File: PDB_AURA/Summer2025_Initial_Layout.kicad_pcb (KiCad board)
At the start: 4 copper layers, 50 x 100 mm, 123 parts, among them J10 532617006, J100 XT30PW-M, J101 USB_C_Receptacle_USB2.0_16P, J3 532617004, J4 TF-CARD_H1.8, J400 Screw_Terminal_01x04, J5 TSW-108-07-G-T, J6 532617004, Q1 BSS138, Q2 BSS138, U1 SI4825DDY-T1-GE3, U101 TPS2115ADRBR, U102 TLV62566DBVR, U103 AP2127N-1.8, U11 ICM-20948, U12 BMP280, U13 MAX-M10S, U2 RFM95W-868S2, U200 ESP32-S3-WROOM-1, U201 USBLC6-2SC6, U3 TPS56C230RJER, U400 DMN6040SSD-13

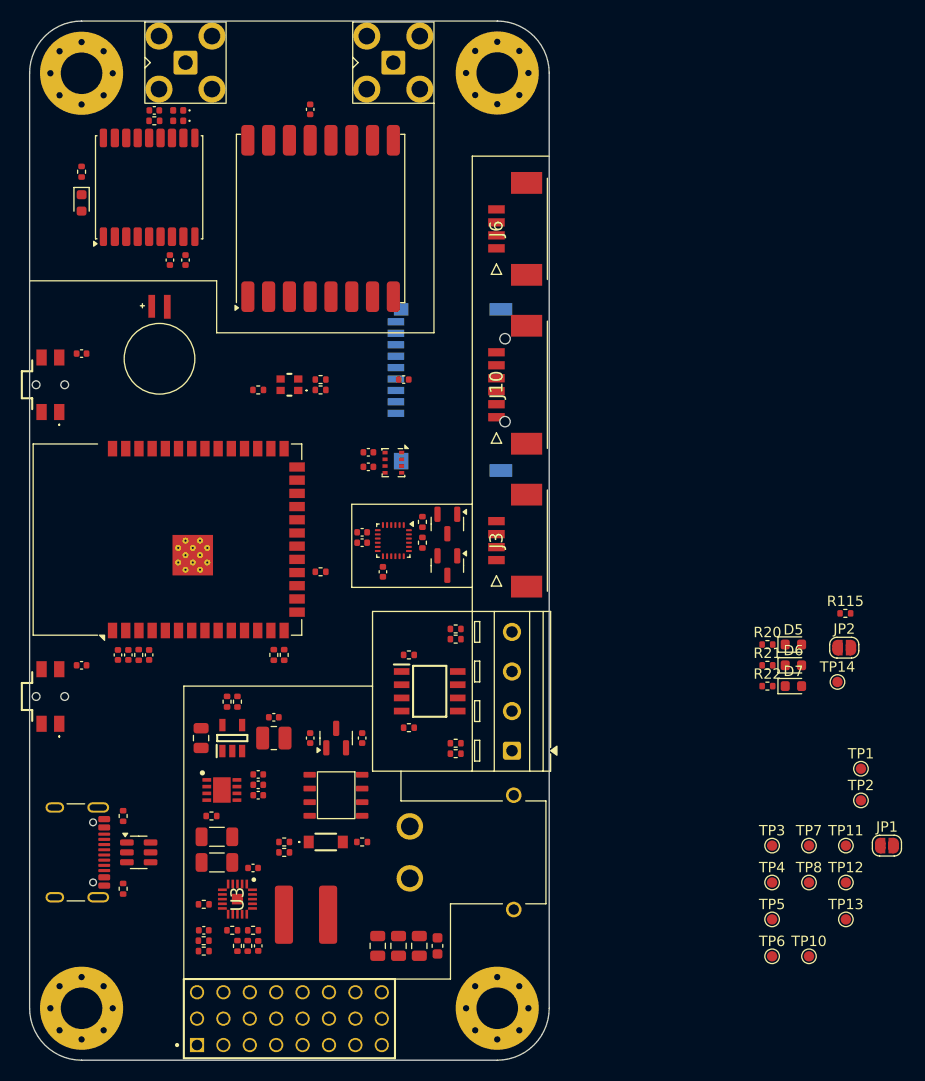
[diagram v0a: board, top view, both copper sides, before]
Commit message: Annotated schematic for PDB
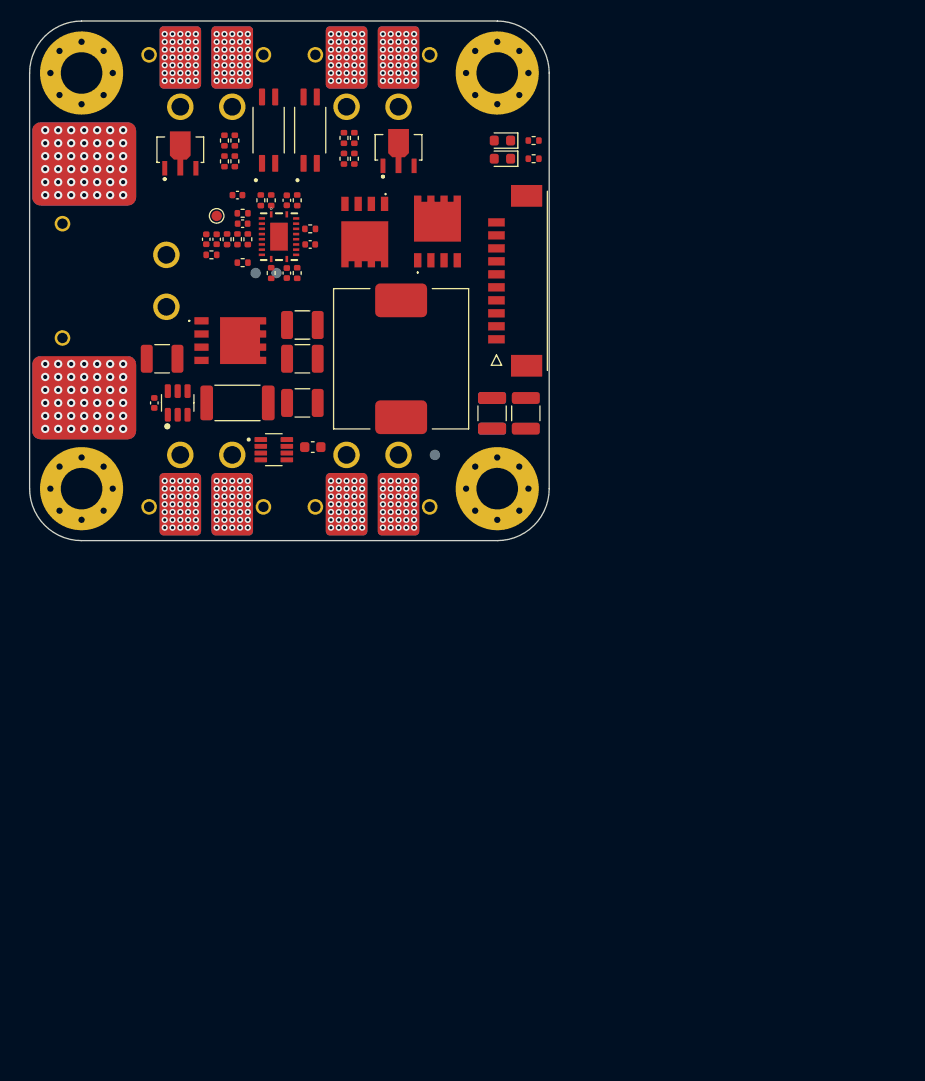
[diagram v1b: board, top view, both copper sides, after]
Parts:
- removed BT1: MS621FE-FL11E, BAT_MS621FE-FL11E:BAT_MS621FE-FL11E
- removed C100, C113, C114: 1u, Capacitor_SMD:C_0402_1005Metric
- removed C101, C102: 22u, Capacitor_SMD:C_1206_3216Metric
- removed C103: 18n, Capacitor_SMD:C_0402_1005Metric
- removed C104, C108, C109, C201, C203, C204, C22, C25, C27, C38, C39, C41, C42, C43, C44, C45: 100n, Capacitor_SMD:C_0402_1005Metric
- removed C105, C106, C107: 22u, Capacitor_SMD:C_0805_2012Metric
- removed C110, C112, C202: 10u, Capacitor_SMD:C_0402_1005Metric
- removed C111: 4u7, Capacitor_SMD:C_0805_2012Metric
- removed C115: 100n, Capacitor_SMD:C_0603_1608Metric
- removed D4, D5, D6, D7: LED, LED_SMD:LED_0603_1608Metric
- removed D503490: ~, Diode_SMD:D_0402_1005Metric
- removed J101: USB_C_Receptacle_USB2.0_16P, Connector_USB:USB_C_Receptacle_GCT_USB4105-xx-A_16P_TopMnt_Horizontal
- removed J400: Screw_Terminal_01x04, TerminalBlock_MetzConnect:TerminalBlock_MetzConnect_Type086_RT03404HBLC_1x04_P3.81mm_Horizontal
- removed JP1, JP2: SolderJumper_2_Bridged, Jumper:SolderJumper-2_P1.3mm_Open_RoundedPad1.0x1.5mm
- removed L100: 1u8, CKST0603:CKST0603-1.5uHM
- removed L101: 2u2, Inductor_SMD:L_1008_2520Metric
- removed L4: 27nH, LED_SMD:LED_0402_1005Metric
- removed R100: 100k, Resistor_SMD:R_0402_1005Metric
- removed R101: 49k, Resistor_SMD:R_0402_1005Metric
- removed R102: 13k, Resistor_SMD:R_0402_1005Metric
- removed R103: 180k, Resistor_SMD:R_0402_1005Metric
- removed R104: 33k, Resistor_SMD:R_0402_1005Metric
- removed R105: 330k, Resistor_SMD:R_0402_1005Metric
- removed R106: 110k, Resistor_SMD:R_0402_1005Metric
- removed R107: 15k, Resistor_SMD:R_0402_1005Metric
- removed R108, R109: 5k1, Resistor_SMD:R_0402_1005Metric
- removed R110: 680R, Resistor_SMD:R_0402_1005Metric
- removed R111: 540k, Resistor_SMD:R_0402_1005Metric
- removed R113, R115, R400, R403: 220k, Resistor_SMD:R_0402_1005Metric
- removed R114, R401, R404: 22k, Resistor_SMD:R_0402_1005Metric
- removed R18, R19, R22: 1k, Resistor_SMD:R_0402_1005Metric
- removed R20, R21: 4k7, Resistor_SMD:R_0402_1005Metric
- removed R25, R26, R27, R402, R405: 10k, Resistor_SMD:R_0402_1005Metric
- removed R36: 100R, Resistor_SMD:R_0402_1005Metric
- removed R37: 120R, Resistor_SMD:R_0402_1005Metric
- removed R38: 270R, Resistor_SMD:R_0402_1005Metric
- removed S3, S4: EVQ-PUC02K, SamacSys_Parts:EVQPUC02K
- removed TP10, TP11, TP12, TP13, TP14, TP5, TP6, TP7, TP8: TestPoint, TestPoint:TestPoint_Pad_D1.0mm
- removed U101: TPS2115ADRBR, SamacSys_Parts:SON65P300X300X100-9N-D
- removed U102: TLV62566DBVR, SamacSys_Parts:SOT95P280X145-5N
- removed U103: AP2127N-1.8, Package_TO_SOT_SMD:SOT-23
- removed U11: ICM-20948, Sensor_Motion:InvenSense_QFN-24_3x3mm_P0.4mm
- removed U12: BMP280, Package_LGA:Bosch_LGA-8_2x2.5mm_P0.65mm_ClockwisePinNumbering
- removed U13: MAX-M10S, RF_GPS:ublox_MAX
- removed U3: TPS56C230RJER, SamacSys_Parts:QFN45P300X300X100-21N-D
- removed U400: DMN6040SSD-13, SamacSys_Parts:SOIC127P600X170-8N
- added C1: 1n, Capacitor_SMD:C_0402_1005Metric, F.Cu at (67.0, 71.0)
- added C10: 47u, Capacitor_SMD:C_1210_3225Metric, F.Cu at (76.2, 86.8)
- added C11: 22u, Capacitor_SMD:C_1210_3225Metric, F.Cu at (76.2, 79.2)
- added C12: 22u, Capacitor_SMD:C_1210_3225Metric, F.Cu at (62.8, 82.5)
- added C14: 22u, Capacitor_SMD:C_1210_3225Metric, F.Cu at (94.5, 87.8)
- added C15: 22u, Capacitor_SMD:C_1210_3225Metric, B.Cu at (94.5, 87.8)
- added C16: 22u, Capacitor_SMD:C_1210_3225Metric, F.Cu at (76.2, 82.5)
- added C2: 8n2, Capacitor_SMD:C_0402_1005Metric, F.Cu at (70.0, 66.8)
- added C3: 100n, Capacitor_SMD:C_0402_1005Metric, F.Cu at (70.5, 69.5)
- added C4: 390p, Capacitor_SMD:C_0402_1005Metric, F.Cu at (68.0, 71.0)
- added C4: 390p, Capacitor_SMD:C_0402_1005Metric, F.Cu at (62.0, 86.8)
- added C5: 100n, Resistor_SMD:R_0402_1005Metric, F.Cu at (77.0, 70.0)
- added C6: 2u2, Capacitor_SMD:C_0402_1005Metric, F.Cu at (77.0, 71.5)
- added C7: 10p, Capacitor_SMD:C_0402_1005Metric, F.Cu at (74.8, 74.2)
- added C8: 100n, Capacitor_SMD:C_0402_1005Metric, F.Cu at (74.8, 67.2)
- added C9: 22u, Capacitor_SMD:C_1210_3225Metric, F.Cu at (97.8, 87.8)
- added J200: 532617010, 532617010:532617010, F.Cu at (94.9, 75.0)
- added J201: XT30PW-F, XT30PWF:XT30PWF, F.Cu at (64.5, 58.2)
- added J202: XT30PW-F, XT30PWF:XT30PWF, F.Cu at (80.5, 58.2)
- added J203: XT30PW-F, XT30PWF:XT30PWF, F.Cu at (69.5, 91.8)
- added J204: XT30PW-F, XT30PWF:XT30PWF, F.Cu at (85.5, 91.8)
- added J7: ~, SOLDER_PAD:PWR_SOLDER_PAD, B.Cu at (80.5, 53.5)
- added J8: ~, SOLDER_PAD:PWR_SOLDER_PAD, B.Cu at (80.5, 96.5)
- added J9: ~, SOLDER_PAD:BAT_SOLDER_PAD, F.Cu at (55.2, 86.2)
- added L1: 1u8, 125CDMCCDS-1R8MC:Untitled, F.Cu at (85.8, 82.5)
- added Q200: HSK10N06, HSK10N06:HSK10N06, F.Cu at (64.5, 63.6)
- added Q201: HSK10N06, HSK10N06:HSK10N06, F.Cu at (85.5, 63.4)
- added Q3: CSD18540Q5B, CSD18540Q5B:CSD18540Q5B, F.Cu at (69.3, 80.8)
- added R1: 18k, Resistor_SMD:R_0402_1005Metric, F.Cu at (70.0, 71.0)
- added R10: 9k1, Resistor_SMD:R_0402_1005Metric, F.Cu at (72.2, 67.2)
- added R11: 2R1, Resistor_SMD:R_0402_1005Metric, F.Cu at (75.8, 67.2)
- added R12: 0m5, Resistor_SMD:R_2512_6332Metric, F.Cu at (70.0, 86.8)
- added R13: 4k7, Resistor_SMD:R_0402_1005Metric, F.Cu at (98.5, 61.5)
- added R2: 3k4, Resistor_SMD:R_0402_1005Metric, F.Cu at (71.0, 71.0)
- added R203: 100R, Resistor_SMD:R_0402_1005Metric, F.Cu at (68.8, 61.5)
- added R204: 10k, Resistor_SMD:R_0402_1005Metric, F.Cu at (81.2, 61.2)
- added R205: 470R, Resistor_SMD:R_0402_1005Metric, F.Cu at (81.2, 63.2)
- added R206: 10k, Resistor_SMD:R_0402_1005Metric, F.Cu at (80.2, 61.2)
- added R207: 100R, Resistor_SMD:R_0402_1005Metric, F.Cu at (80.2, 63.2)
- added R3: 1k47, Resistor_SMD:R_0402_1005Metric, F.Cu at (69.0, 71.0)
- added R4: 4k7, Resistor_SMD:R_0402_1005Metric, F.Cu at (70.5, 68.5)
- added R5: 249R, Resistor_SMD:R_0402_1005Metric, F.Cu at (67.5, 72.5)
- added R6: 20k, Resistor_SMD:R_0402_1005Metric, F.Cu at (70.5, 73.2)
- added R7: 576R, Resistor_SMD:R_0402_1005Metric, F.Cu at (75.8, 74.2)
- added R8: 4k7, Resistor_SMD:R_0402_1005Metric, F.Cu at (73.2, 74.2)
- added R9: 35k7, Resistor_SMD:R_0402_1005Metric, F.Cu at (73.2, 67.2)
- added U202: INA219AIDCNR, INA219AIDCNR:SOT65P280X145-8N, F.Cu at (73.5, 91.2)
- C200: value 22u -> 100n; footprint Capacitor_SMD:C_0402_1005Metric -> Capacitor_SMD:C_0603_1608Metric
- D1: value NH-B2020RGBA-HF -> LED; footprint SamacSys_Parts:NHB2020RGBAHF -> LED_SMD:LED_0603_1608Metric
- D101: value MMSZ5242B -> LED; footprint SamacSys_Parts:MMSZ5252B -> LED_SMD:LED_0603_1608Metric
- J1, J2: footprint SMA_Connector:SMA_Connector -> SOLDER_PAD:PWR_SOLDER_PAD; moved to B.Cu
- J10: value 532617006 -> ~; footprint SamacSys_Parts:532617006 -> SOLDER_PAD:BAT_SOLDER_PAD
- J100: footprint SamacSys_Parts:XT30PWM -> XT30PWM:XT30PWM
- J3, J6: value 532617004 -> ~; footprint SamacSys_Parts:532617004 -> SOLDER_PAD:PWR_SOLDER_PAD; moved to B.Cu
- J4: value TF-CARD_H1.8 -> ~; footprint SamacSys_Parts:TFCARDH18 -> SOLDER_PAD:PWR_SOLDER_PAD
- J5: value TSW-108-07-G-T -> ~; footprint SAMTEC_TSW-108-07-G-T:SAMTEC_TSW-108-07-G-T -> SOLDER_PAD:PWR_SOLDER_PAD; moved to B.Cu
- Q1: value BSS138 -> CSD18540Q5B; footprint Package_TO_SOT_SMD:SOT-23 -> CSD18540Q5B:CSD18540Q5B
- Q2: value BSS138 -> CSD18510Q5B; footprint Package_TO_SOT_SMD:SOT-23 -> CSD18510Q5B:CSD18540Q5BT
- R112: value 120k -> 4k7
- R201: value 0R -> 470R
- R202: value 0R -> 10k
- TP1, TP3, TP4: moved to B.Cu
- U1: value SI4825DDY-T1-GE3 -> LM25145RGYR; footprint SI4825DDY-T1-GE3:SI4825DDY-T1-GE3 -> LM24145RGYR:RGY0020B
- U2: value RFM95W-868S2 -> LM74700; footprint RF_Module:HOPERF_RFM9XW_SMD -> Package_TO_SOT_SMD:SOT-23-6
- U200: value ESP32-S3-WROOM-1 -> LTV-217-B-G; footprint RF_Module:ESP32-S3-WROOM-1 -> LTV-217-B-G:SOIC127P700X210-4N
- U201: value USBLC6-2SC6 -> LTV-217-B-G; footprint Package_TO_SOT_SMD:SOT-23-6 -> LTV-217-B-G:SOIC127P700X210-4N
- moved H3 90.0 mm to (55.0, 55.0)
- moved H4 90.0 mm to (95.0, 55.0)
- moved TP2 83.7 mm to (68.0, 68.8)
- moved TP1 75.3 mm to (71.8, 74.2), turned to 180 degrees
- moved TP3 72.9 mm to (73.8, 74.2), turned to 180 degrees
- moved U201 71.4 mm to (77.0, 60.5), turned to 90 degrees
- moved D101 67.9 mm to (95.5, 63.2), turned to 180 degrees
- moved J100 65.3 mm to (57.2, 75.0), turned to 90 degrees
- moved R112 60.0 mm to (98.5, 63.2), turned to 180 degrees
- moved H1 56.6 mm to (55.0, 95.0)
- moved H2 56.6 mm to (95.0, 95.0)
- moved J3 55.6 mm to (64.5, 53.5), turned to 180 degrees
- moved U1 54.0 mm to (74.0, 70.8), turned to 0 degrees
- moved TP4 52.4 mm to (89.0, 91.8), turned to 180 degrees
- moved J5 50.6 mm to (85.5, 96.5), turned to 180 degrees
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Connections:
- D1 pad 1: LED_R -> /100_Power/5V_LED
- D1 pad 2: LED_B -> +5V
- D101 pad 1: +BATT_FILT -> /100_Power/VBAT_LED
- D101 pad 2: /Power/rvrs_plr -> +BATT_FILT
- J1 pad 1: /RF_Peripherals/LORA_ANT -> +BATT_FILT
- J10 pad 1: +3V3 -> GND
- J2 pad 1: /RF_Peripherals/GPS_RF_IN -> GND
- J3 pad 1: +3V3 -> +BATT_FILT
- J4 pad 1: unconnected-(J4-DAT2-Pad1) -> GND
- J6 pad 1: TCK -> GND
- Q1 pad 1: +1V8 -> /100_Power/5V_HO
- Q1 pad 2: /Digital_Peripherals/SCL_1V8 -> +BATT_FILT
- Q1 pad 3: SCL -> /100_Power/5V_SW
- Q2 pad 1: +1V8 -> /100_Power/5V_LO
- Q2 pad 2: /Digital_Peripherals/SDA_1V8 -> /100_Power/5V_SW
- Q2 pad 3: SDA -> GND
- R112 pad 2: /Power/FB_3V3 -> /100_Power/VBAT_LED
- R200 pad 1: /ESP32/EN -> GND
- R200 pad 2: +3V3 -> MSFT_1
- R201 pad 1: /ESP32/USB_MCU_D- -> /200_Connectors/MSFT_1_R
- R201 pad 2: /ESP32/D- -> MSFT_1
- R202 pad 1: /ESP32/USB_MCU_D+ -> GND
- R202 pad 2: /ESP32/D+ -> /200_Connectors/VGS_CH1
- TP1 pad 1: /Digital_Peripherals/SCL_1V8 -> /100_Power/5V_SYNCOUT
- TP2 pad 1: /Digital_Peripherals/SDA_1V8 -> /100_Power/5V_FB
- TP3 pad 1: /Power/PGOOD -> /100_Power/5V_PGOOD
- TP4 pad 1: /Power/EN_5V -> +5V
- U1 pad 1: +BATT -> /100_Power/5V_EN
- U1 pad 2: +BATT -> /100_Power/5V_RT
- U1 pad 3: +BATT -> /100_Power/5V_SS
- U1 pad 4: /Power/rvrs_plr -> /100_Power/COMP_FB_C
- U1 pad 5: +BATT_FILT -> /100_Power/5V_FB
- U1 pad 6: +BATT_FILT -> GND
- U1 pad 7: +BATT_FILT -> /100_Power/5V_SYNCOUT
- U1 pad 8: +BATT_FILT -> /100_Power/5V_SYNCIN
- U2 pad 1: GND -> /100_Power/VCAP
- U2 pad 2: MISO -> GND
- U2 pad 3: MOSI -> +BATT
- U2 pad 4: SCK -> INA_IN+
- U2 pad 5: LORA_CS -> /100_Power/PLR_G
- U2 pad 6: LORA_RST -> +BATT
- U200 pad 1: GND -> /200_Connectors/MSFT_1_R
- U200 pad 2: +3V3 -> GND
- U200 pad 3: /ESP32/EN -> /200_Connectors/VGS_CH1
- U200 pad 4: SERVO_4 -> +5V
- U201 pad 1: USB_D- -> /200_Connectors/MSFT_2_R
- U201 pad 3: USB_D+ -> /200_Connectors/VGS_CH2
- U201 pad 4: /ESP32/USB_MCU_D+ -> +5V
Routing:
- net GND: vias 0 -> 182
- net +BATT_FILT: vias 0 -> 140
- net +BATT: vias 0 -> 42
- removed copper zone on In1.Cu, net GND
- removed copper zone on In2.Cu, net GND
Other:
- board size 50 x 100 mm -> 50 x 50 mm
- board text added: "J1"
